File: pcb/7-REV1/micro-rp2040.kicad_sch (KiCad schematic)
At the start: 58 parts, among them J201 Conn_01x03, J202 TYPE-C-31-M-12, Q1 MMBT7002K, Q2 MMBT7002K, SW101 TS3425BA 098 2.5H 250gf, SW102 TS3315A 250gf 025, U1 RP2350B, U102 W25Q128JVSIQ, U105 MT29F1G01ABAFDWB, U3 TLV74311PDBVR, U401 ME6211A33PG-N, U8 APS6404L-3SQR-ZR, Y101 ABM8-272-T3

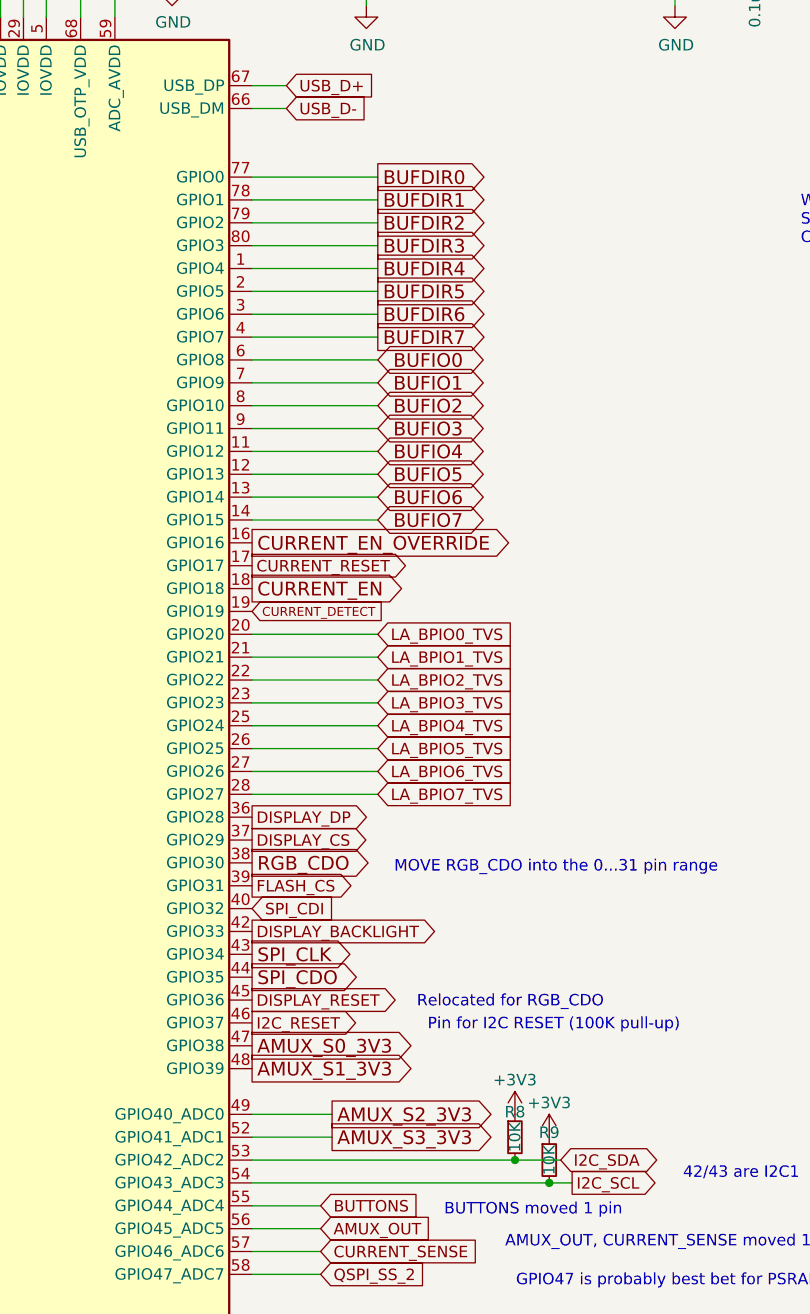
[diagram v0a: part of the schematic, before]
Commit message: Move CURRENT_DETECT back to AMUX
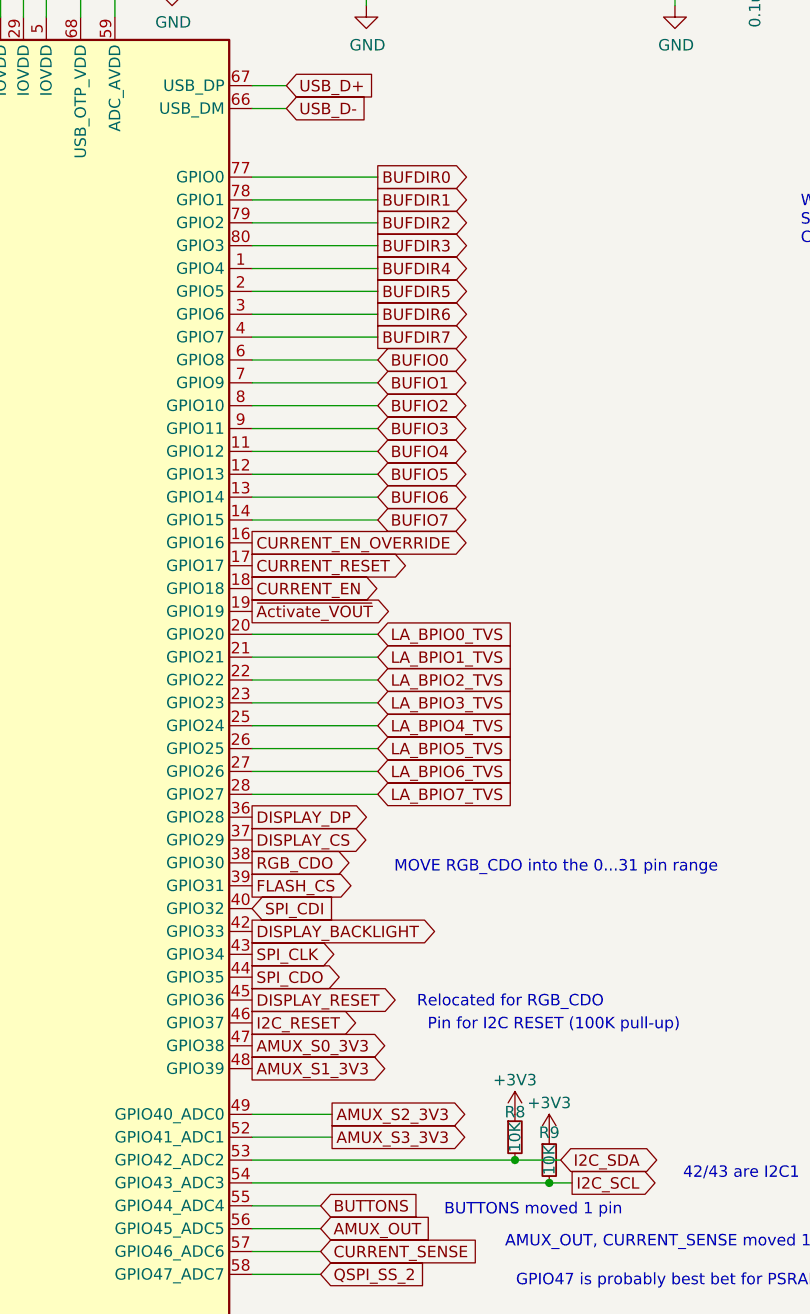
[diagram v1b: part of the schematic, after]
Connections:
- net CURRENT_DETECT renamed ~{Activate_VOUT}
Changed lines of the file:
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@@
 		(effects
 			(font
-				(size 1.524 1.524)
+				(size 1.27 1.27)
 			)
 			(justify left)
@@
 		(effects
 			(font
-				(size 1.524 1.524)
+				(size 1.27 1.27)
 			)
 			(justify left)
@@
 		(effects
 			(font
-				(size 1.524 1.524)
+				(size 1.27 1.27)
 			)
 			(justify left)
@@
 		(effects
 			(font
-				(size 1.524 1.524)
+				(size 1.27 1.27)
 			)
 			(justify left)
@@
 		(effects
 			(font
-				(size 1.524 1.524)
+				(size 1.27 1.27)
 			)
 			(justify left)
@@
 		(effects
 			(font
-				(size 1.524 1.524)
+				(size 1.27 1.27)
 			)
 			(justify left)
@@
 		)
 	)
-	(global_label "CURRENT_DETECT"
-		(shape input)
+	(global_label "~{Activate_VOUT}"
+		(shape output)
 		(at 297.18 129.54 0)
 		(effects
 			(font
-				(size 0.9906 0.9906)
+				(size 1.27 1.27)
 			)
 			(justify left)
@@
 		(effects
 			(font
-				(size 1.524 1.524)
+				(size 1.27 1.27)
 			)
 			(justify left)
@@
 		(effects
 			(font
-				(size 1.524 1.524)
+				(size 1.27 1.27)
 			)
 			(justify left)
@@
 		(effects
 			(font
-				(size 1.524 1.524)
+				(size 1.27 1.27)
 			)
 			(justify left)
@@
 		(effects
 			(font
-				(size 1.524 1.524)
+				(size 1.27 1.27)
 			)
 			(justify left)
@@
 		(effects
 			(font
-				(size 1.524 1.524)
+				(size 1.27 1.27)
 			)
 			(justify left)
@@
 		(effects
 			(font
-				(size 1.524 1.524)
+				(size 1.27 1.27)
 			)
 			(justify left)
@@
 		(effects
 			(font
-				(size 1.524 1.524)
+				(size 1.27 1.27)
 			)
 			(justify left)
@@
 		(effects
 			(font
-				(size 1.524 1.524)
+				(size 1.27 1.27)
 			)
 			(justify left)
@@
 		(effects
 			(font
-				(size 1.524 1.524)
+				(size 1.27 1.27)
 			)
 			(justify left)
@@
 		(effects
 			(font
-				(size 1.524 1.524)
+				(size 1.27 1.27)
 			)
 			(justify left)
@@
 		(effects
 			(font
+				(size 1.27 1.27)
+			)
+			(justify left)
+		)
+		(property "Intersheetrefs" "${INTERSHEET_REFS}"
+			(at 311.15 101.6 0)
+			(effects
+				(font
+					(size 1.27 1.27)
+				)
+				(hide yes)
+			)
+		)
+	)
+	(global_label "SWDIO"
+		(shape bidirectional)
+		(at 161.29 54.61 180)
+		(effects
+			(font
 				(size 1.524 1.524)
 			)
-			(justify left)
-		)
-		(property "Intersheetrefs" "${INTERSHEET_REFS}"
-			(at 311.15 101.6 0)
-			(effects
-				(font
-					(size 1.27 1.27)
-				)
-				(hide yes)
-			)
-		)
-	)
-	(global_label "SWDIO"
-		(shape bidirectional)
-		(at 161.29 54.61 180)
+			(justify right)
+		)
+		(property "Intersheetrefs" "${INTERSHEET_REFS}"
+			(at 161.29 54.61 0)
+			(effects
+				(font
+					(size 1.27 1.27)
+				)
+				(hide yes)
+			)
+		)
+	)
+	(global_label "BUFDIR4"
+		(shape output)
+		(at 311.15 91.44 0)
+		(effects
+			(font
+				(size 1.27 1.27)
+			)
+			(justify left)
+		)
+		(property "Intersheetrefs" "${INTERSHEET_REFS}"
+			(at 311.15 91.44 0)
+			(effects
+				(font
+					(size 1.27 1.27)
+				)
+				(hide yes)
+			)
+		)
+	)
+	(global_label "BUFDIR5"
+		(shape output)
+		(at 311.15 93.98 0)
+		(effects
+			(font
+				(size 1.27 1.27)
+			)
+			(justify left)
+		)
+		(property "Intersheetrefs" "${INTERSHEET_REFS}"
+			(at 311.15 93.98 0)
+			(effects
+				(font
+					(size 1.27 1.27)
+				)
+				(hide yes)
+			)
+		)
+	)
+	(global_label "BUFDIR7"
+		(shape output)
+		(at 311.15 99.06 0)
+		(effects
+			(font
+				(size 1.27 1.27)
+			)
+			(justify left)
+		)
+		(property "Intersheetrefs" "${INTERSHEET_REFS}"
+			(at 311.15 99.06 0)
+			(effects
+				(font
+					(size 1.27 1.27)
+				)
+				(hide yes)
+			)
+		)
+	)
+	(global_label "USB_D+"
+		(shape output)
+		(at 107.95 46.99 0)
 		(effects
 			(font
 				(size 1.524 1.524)
 			)
-			(justify right)
-		)
-		(property "Intersheetrefs" "${INTERSHEET_REFS}"
-			(at 161.29 54.61 0)
-			(effects
-				(font
-					(size 1.27 1.27)
-				)
-				(hide yes)
-			)
-		)
-	)
-	(global_label "BUFDIR4"
-		(shape output)
-		(at 311.15 91.44 0)
-		(effects
-			(font
-				(size 1.524 1.524)
-			)
-			(justify left)
-		)
-		(property "Intersheetrefs" "${INTERSHEET_REFS}"
-			(at 311.15 91.44 0)
-			(effects
-				(font
-					(size 1.27 1.27)
-				)
-				(hide yes)
-			)
-		)
-	)
-	(global_label "BUFDIR5"
-		(shape output)
-		(at 311.15 93.98 0)
-		(effects
-			(font
-				(size 1.524 1.524)
-			)
-			(justify left)
-		)
-		(property "Intersheetrefs" "${INTERSHEET_REFS}"
-			(at 311.15 93.98 0)
-			(effects
-				(font
-					(size 1.27 1.27)
-				)
-				(hide yes)
-			)
-		)
-	)
-	(global_label "BUFDIR7"
-		(shape output)
-		(at 311.15 99.06 0)
-		(effects
-			(font
-				(size 1.524 1.524)
-			)
-			(justify left)
-		)
-		(property "Intersheetrefs" "${INTERSHEET_REFS}"
-			(at 311.15 99.06 0)
-			(effects
-				(font
-					(size 1.27 1.27)
-				)
-				(hide yes)
-			)
-		)
-	)
-	(global_label "USB_D+"
-		(shape output)
-		(at 107.95 46.99 0)
-		(effects
-			(font
-				(size 1.524 1.524)
-			)
 			(justify left)
 		)
@@
 		(effects
 			(font
-				(size 1.524 1.524)
+				(size 1.27 1.27)
 			)
 			(justify left)
@@
 		(effects
 			(font
-				(size 1.524 1.524)
+				(size 1.27 1.27)
 			)
 			(justify left)
@@
 		(effects
 			(font
-				(size 1.524 1.524)
+				(size 1.27 1.27)
 			)
 			(justify left)
@@
 		(effects
 			(font
-				(size 1.524 1.524)
+				(size 1.27 1.27)
 			)
 			(justify left)
@@
 		(effects
 			(font
-				(size 1.524 1.524)
-			)
-			(justify left)
+				(size 1.27 1.27)
+			)
+			(justify left)

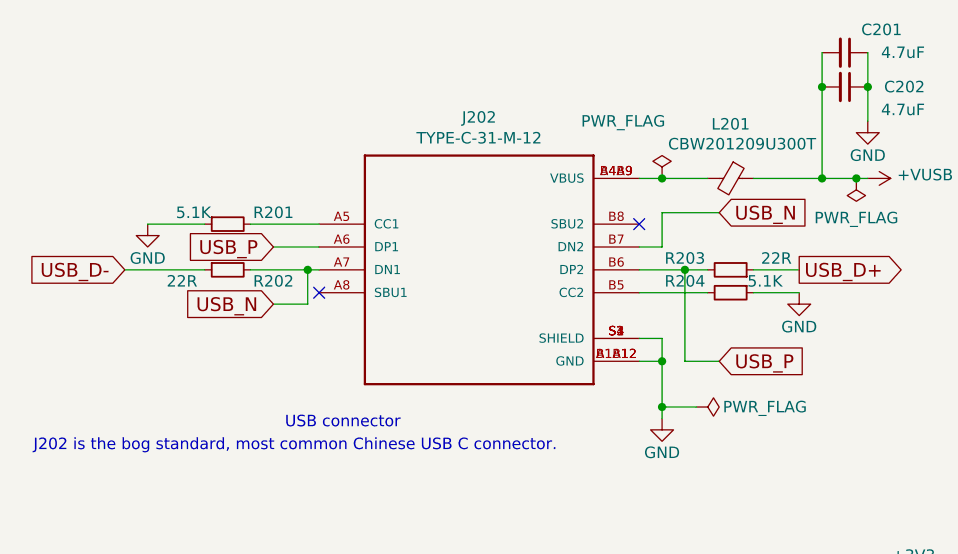
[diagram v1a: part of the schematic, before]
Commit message: change to 27R usb termination resistors as recommended by RasPi (7-REV1)
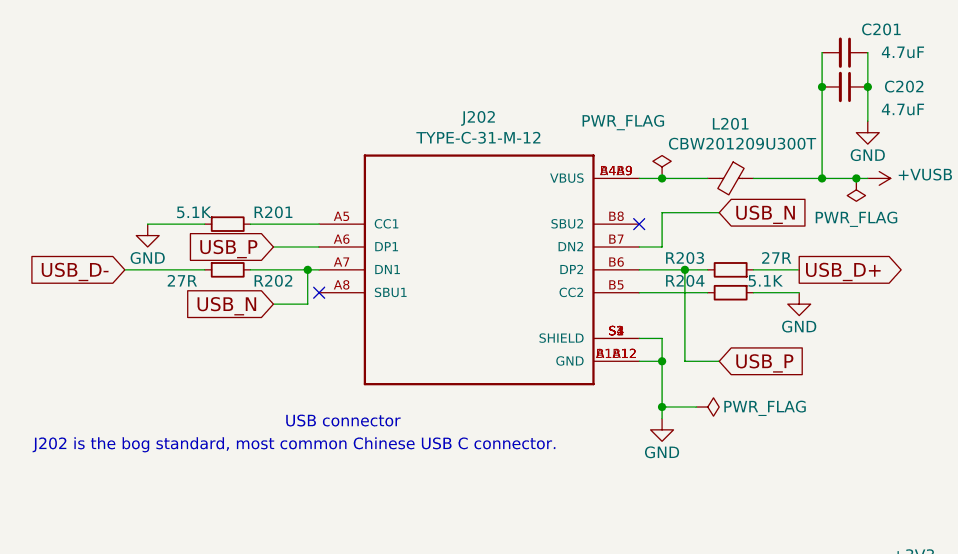
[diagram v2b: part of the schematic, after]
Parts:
- R202, R203: value 22R -> 27R
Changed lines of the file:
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@@
 			)
 		)
-		(property "Value" "22R"
+		(property "Value" "27R"
 			(at 39.37 48.26 90)
 			(effects
@@
 			)
 		)
-		(property "Value" "22R"
+		(property "Value" "27R"
 			(at 105.41 45.72 90)
 			(effects

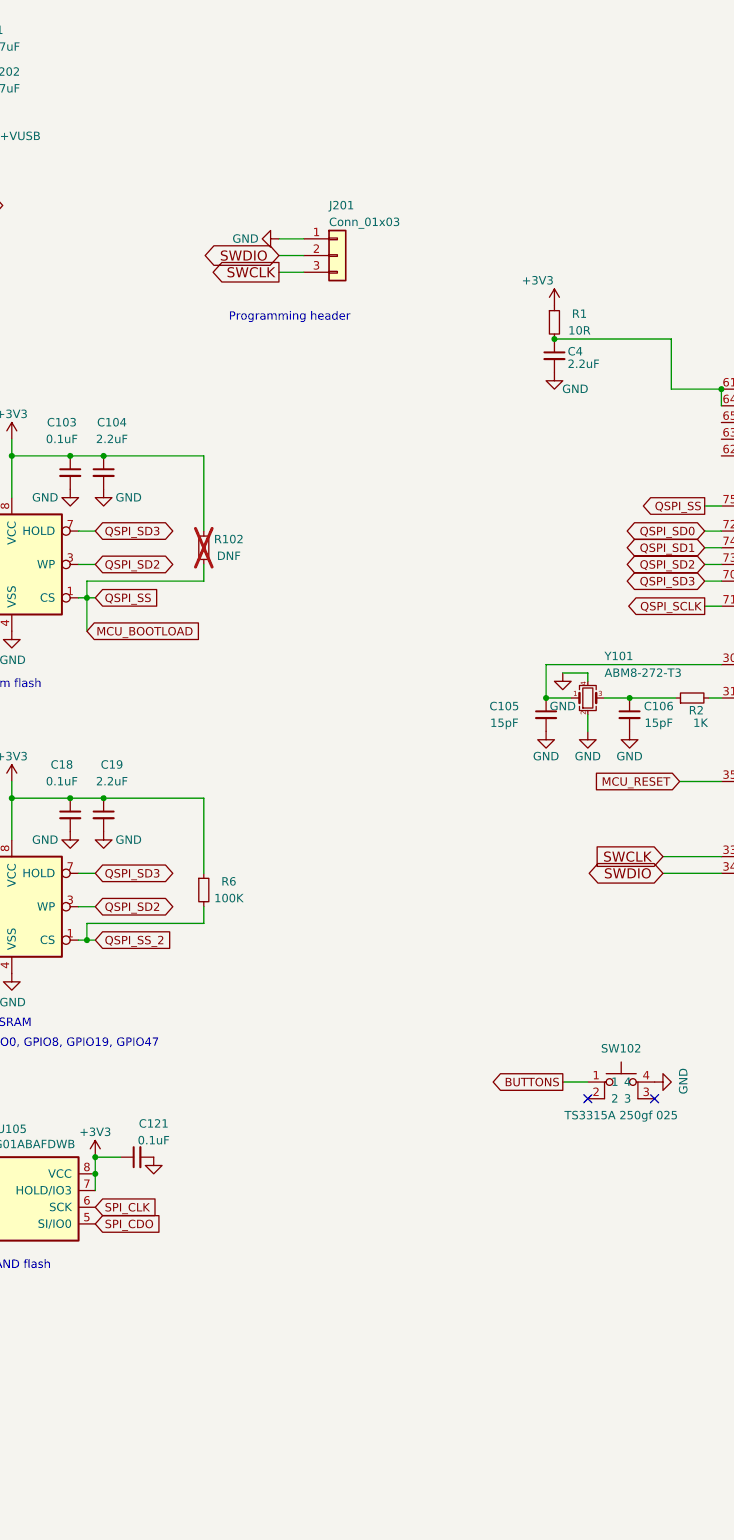
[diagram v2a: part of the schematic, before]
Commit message: add ESD protection for the USB port too
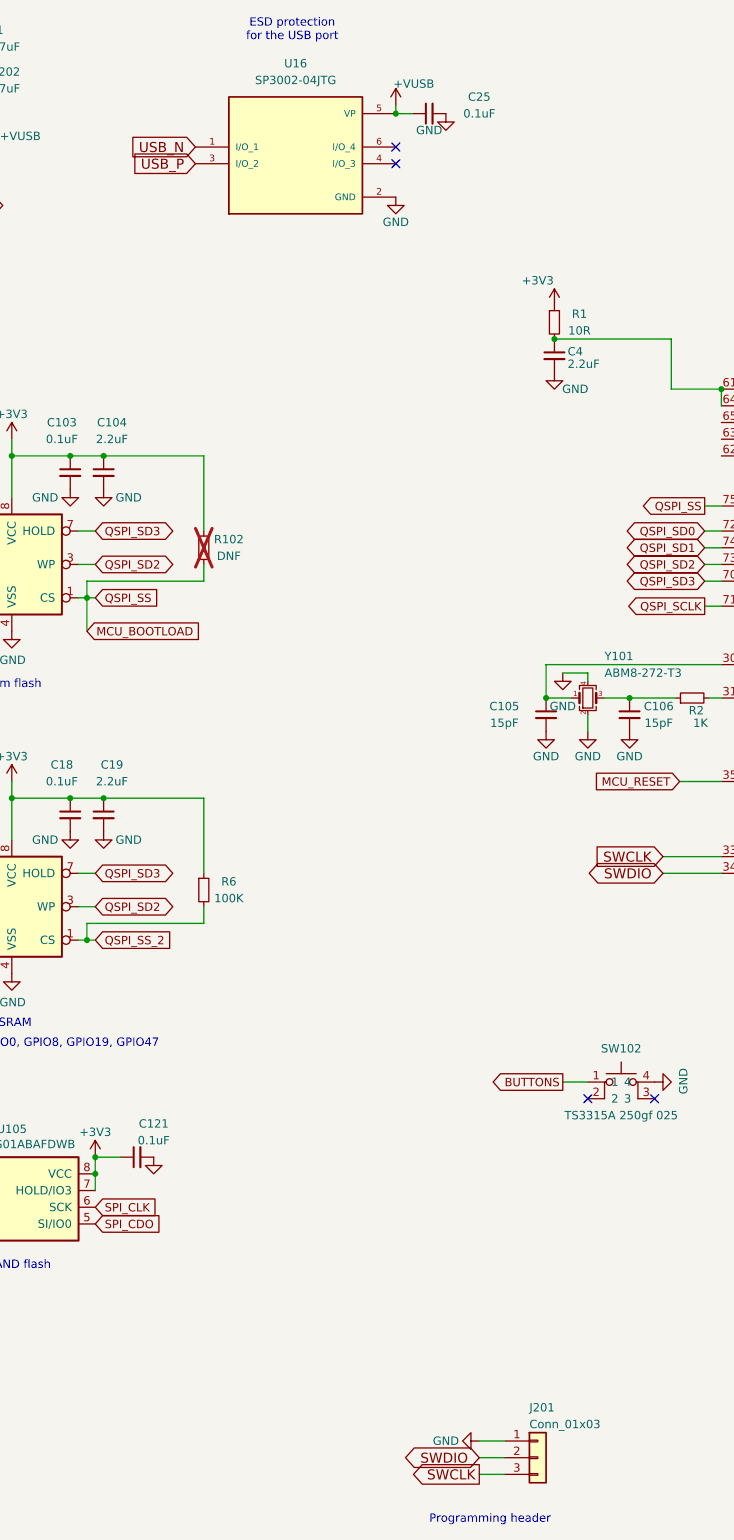
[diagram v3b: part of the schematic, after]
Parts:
- added C25: 0.1uF, Capacitor_SMD:C_0402_1005Metric, symbol Device:C_Small
- added U16: SP3002-04JTG, Package_TO_SOT_SMD:SOT-363_SC-70-6, symbol IP4220CZ6F:IP4220CZ6F
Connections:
- net +VUSB: now also C25.1, U16.5 (VP)
- net GND: now also C25.2, U16.2 (GND)
- net USB_N: now also U16.1 (I/O_1)
- net USB_P: now also U16.3 (I/O_2)
- no-connect marks 4 -> 6
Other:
- note added: "ESD protection for the USB port"
- moved on the sheet: J201

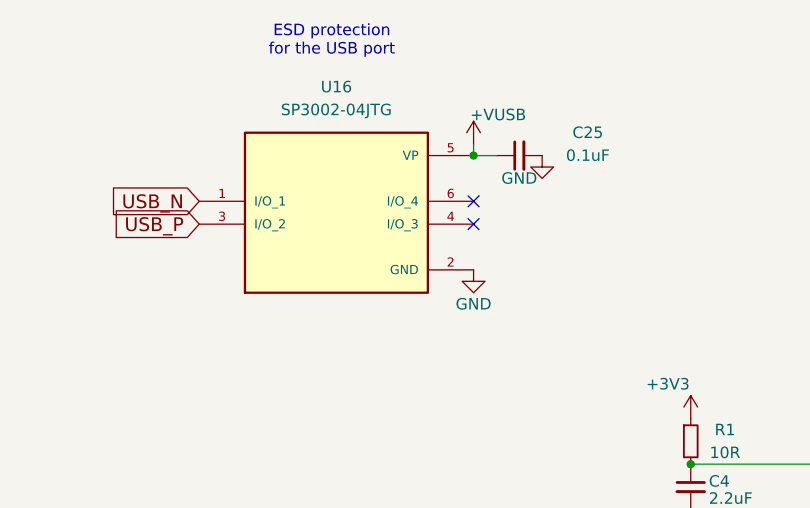
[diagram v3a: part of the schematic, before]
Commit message: change the decoupling caps for the SP3002-04JTG TVS diodes to 4.7µF
Lower impedanced decoupling, can absorb more energy fast
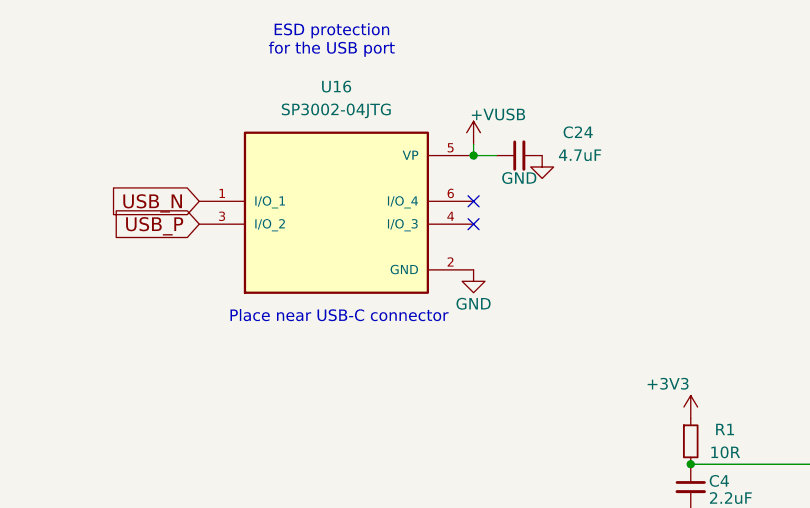
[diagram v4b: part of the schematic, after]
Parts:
- removed C25: 0.1uF, Capacitor_SMD:C_0402_1005Metric, symbol Device:C_Small
- added C24: 4.7uF, Capacitor_SMD:C_0402_1005Metric, symbol Device:C_Small
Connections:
- net +VUSB: now also C24.1
- net GND: now also C24.2
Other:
- note added: "Place near USB-C connector"
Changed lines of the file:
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@@
 		)
 	)
+	(text "Place near USB-C connector"
+		(exclude_from_sim no)
+		(at 164.084 51.054 0)
+		(effects
+			(font
+				(size 1.27 1.27)
+			)
+		)
+	)
 	(text "Power supply"
 		(exclude_from_sim no)
@@
 		(on_board yes)
 		(dnp no)
-		(property "Reference" "C25"
-			(at 191.77 30.48 90)
+		(property "Reference" "C24"
+			(at 188.976 30.48 90)
 			(effects
 				(font
 					(size 1.27 1.27)
 				)
+				(justify right)
 			)
 		)
-		(property "Value" "0.1uF"
-			(at 191.77 33.02 90)
+		(property "Value" "4.7uF"
+			(at 188.468 33.02 90)
 			(effects
 				(font
 					(size 1.27 1.27)
 				)
+				(justify right)
 			)
 		)
@@
 			)
 		)
-		(property "RMB" "0.00628"
+		(property "RMB" "0.037726"
 			(at 184.15 33.02 0)
 			(effects
@@
 			(project "7-REV1"
 				(path "/1f56410a-eaac-4444-b0f7-cfd3531e22ac/00000000-0000-0000-0000-000060c8ec36"
-					(reference "C25")
+					(reference "C24")
 					(unit 1)
 				)
